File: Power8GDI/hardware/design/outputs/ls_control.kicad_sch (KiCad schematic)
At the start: 6 parts, among them U1140 SN74LVC1G17QDBVRQ1

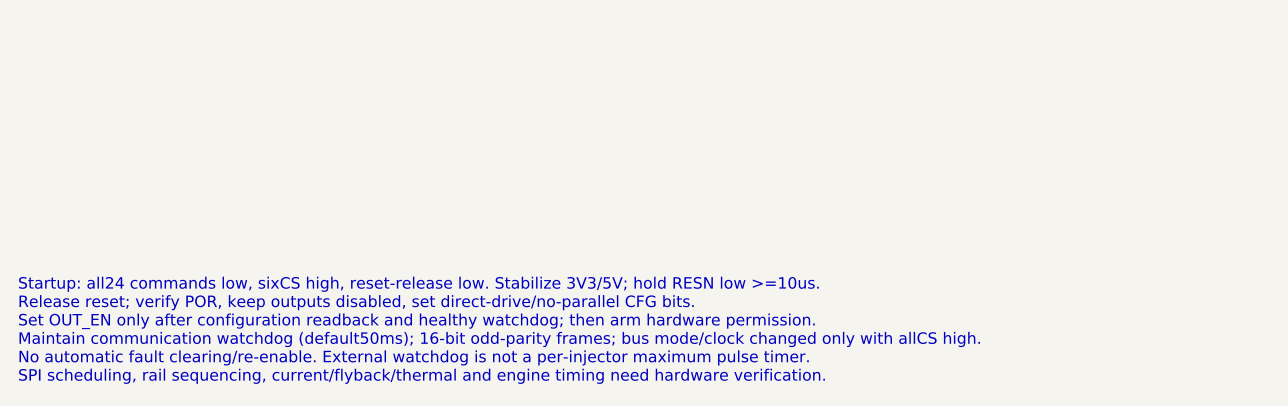
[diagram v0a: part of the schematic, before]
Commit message: Redesign sport target as six DI/PI channels with two motors and one lambda
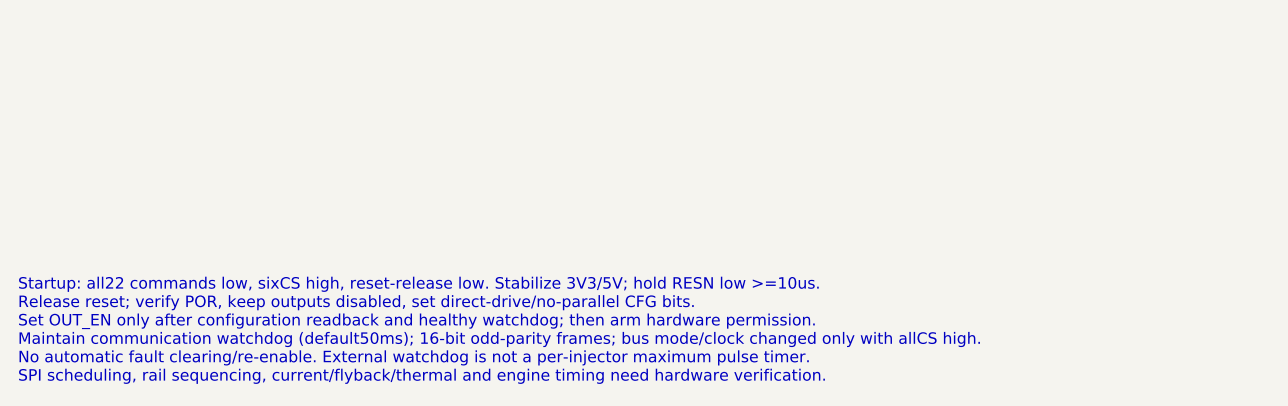
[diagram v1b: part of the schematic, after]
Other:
- note added: "Startup: all22 commands low, sixCS high, reset-release low. Stabilize 3V3/5V; hold RESN low >=10us. Release reset; verify POR, keep outputs disabled, set direct-drive/no-parallel CFG bits. Set OUT_EN only after configuration readback and healthy watchdog; then arm hardware permission. Maintain communication watchdog (default50ms); 16-bit odd-parity frames; bus mode/clock changed only with allCS h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"
- note removed: "Startup: all24 commands low, sixCS high, reset-release low. Stabilize 3V3/5V; hold RESN low >=10us. Release reset; verify POR, keep outputs disabled, set direct-drive/no-parallel CFG bits. Set OUT_EN only after configuration readback and healthy watchdog; then arm hardware permission. Maintain communication watchdog (default50ms); 16-bit odd-parity frames; bus mode/clock changed only with allCS h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"
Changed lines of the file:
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@@
 (wire (pts (xy 260.35 153.67) (xy 260.35 161.29)) (stroke (width 0) (type default)))
 (global_label "LS_SPI_MOSI" (shape bidirectional) (at 260.35 161.29 90) (effects (font (size 1.016 1.016)) (justify right bottom)))
-(text "Startup: all24 commands low, sixCS high, reset-release low. Stabilize 3V3/5V; hold RESN low >=10us.\nRelease reset; verify POR, keep outputs disabled, set direct-drive/no-parallel CFG bits.\nSet OUT_EN only after configuration readback and healthy watchdog; then arm hardware permission.\nMaintain communication watchdog (default50ms); 16-bit odd-parity frames; bus mode/clock changed only with allCS high.\nNo automatic fault clearing/re-enable. External watchdog is not a per-injector maximum pulse timer.\nSPI scheduling, rail sequencing, current/flyback/thermal and engine timing need hardware verification." (at 25.4 200 0) (effects (font (size 1.27 1.27)) (justify left top)))
+(text "Startup: all22 commands low, sixCS high, reset-release low. Stabilize 3V3/5V; hold RESN low >=10us.\nRelease reset; verify POR, keep outputs disabled, set direct-drive/no-parallel CFG bits.\nSet OUT_EN only after configuration readback and healthy watchdog; then arm hardware permission.\nMaintain communication watchdog (default50ms); 16-bit odd-parity frames; bus mode/clock changed only with allCS high.\nNo automatic fault clearing/re-enable. External watchdog is not a per-injector maximum pulse timer.\nSPI scheduling, rail sequencing, current/flyback/thermal and engine timing need hardware verification." (at 25.4 200 0) (effects (font (size 1.27 1.27)) (justify left top)))
 (sheet_instances (path "/" (page "1"))))

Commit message: Review B58 injector power stage and bind selected GDI6 BOM
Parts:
- C1241: Hardware_Qualification (none) -> BOARD_QUALIFICATION_PENDING; MPN (none) -> C0603C104K5RACTU; Manufacturer (none) -> KEMET; Procurement_Status (none) -> SELECTED_CATALOG_ITEM; Purchase_Released (none) -> false; Selection_Gaps (none) -> []; Selection_ID (none) -> SEL-6bf9727c4e40; Selection_Ratings (none) -> {"capacitance_pf": 100000, "dielectric": "X7R", "rated_volt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; Selection_Source_URLs (none) -> https://search.kemet.com/download/specsheet/C0603C104K5RACTU
- R1241: Hardware_Qualification (none) -> BOARD_QUALIFICATION_PENDING; MPN (none) -> CRCW0603100KFKEA; Manufacturer (none) -> Vishay; Procurement_Status (none) -> SELECTED_FAMILY_CODE; Purchase_Released (none) -> false; Selection_Gaps (none) -> []; Selection_ID (none) -> SEL-4e3f06cba0aa; Selection_Ratings (none) -> {"aec_q200": true, "derating": "Use manufacturer power vers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; Selection_Source_URLs (none) -> https://www.vishay.com/docs/20035/dcrcwe3.pdf
- R1242: Hardware_Qualification (none) -> BOARD_QUALIFICATION_PENDING; MPN (none) -> CRCW06031K00FKEA; Manufacturer (none) -> Vishay; Procurement_Status (none) -> SELECTED_FAMILY_CODE; Purchase_Released (none) -> false; Selection_Gaps (none) -> []; Selection_ID (none) -> SEL-38197231a947; Selection_Ratings (none) -> {"aec_q200": true, "derating": "Use manufacturer power vers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; Selection_Source_URLs (none) -> https://www.vishay.com/docs/20035/dcrcwe3.pdf
- R1243, R1244: Hardware_Qualification (none) -> BOARD_QUALIFICATION_PENDING; MPN (none) -> CRCW060333R0FKEA; Manufacturer (none) -> Vishay; Procurement_Status (none) -> SELECTED_FAMILY_CODE; Purchase_Released (none) -> false; Selection_Gaps (none) -> []; Selection_ID (none) -> SEL-9662b03041dd; Selection_Ratings (none) -> {"aec_q200": true, "derating": "Use manufacturer power vers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; Selection_Source_URLs (none) -> https://www.vishay.com/docs/20035/dcrcwe3.pdf
- U1140: Hardware_Qualification (none) -> PINOUT_RATINGS_AND_DELIVERY_SUFFIX_REVIEW_PENDING; MPN (none) -> SN74LVC1G17QDBVRQ1; Manufacturer (none) -> Texas Instruments; Procurement_Status (none) -> REFERENCE_MPN_RETAINED; Purchase_Released (none) -> false; Selection_Gaps (none) -> ["Existing schematic MPN retained. Complete circuit rating/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; Selection_ID (none) -> SEL-ecf3e6662afb; Selection_Ratings (none) -> {}; Selection_Source_URLs (none) -> https://www.ti.com/product/SN74LVC1G17-Q1/part-details/SN74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
